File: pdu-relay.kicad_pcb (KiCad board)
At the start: 2 copper layers, 55 x 40 mm, 15 parts, among them J1 L_IN, J2 N, J3 L_OUT, J4 EXT_ON, K2 G2RL-1A-E DC5, Q1 BSS84PW

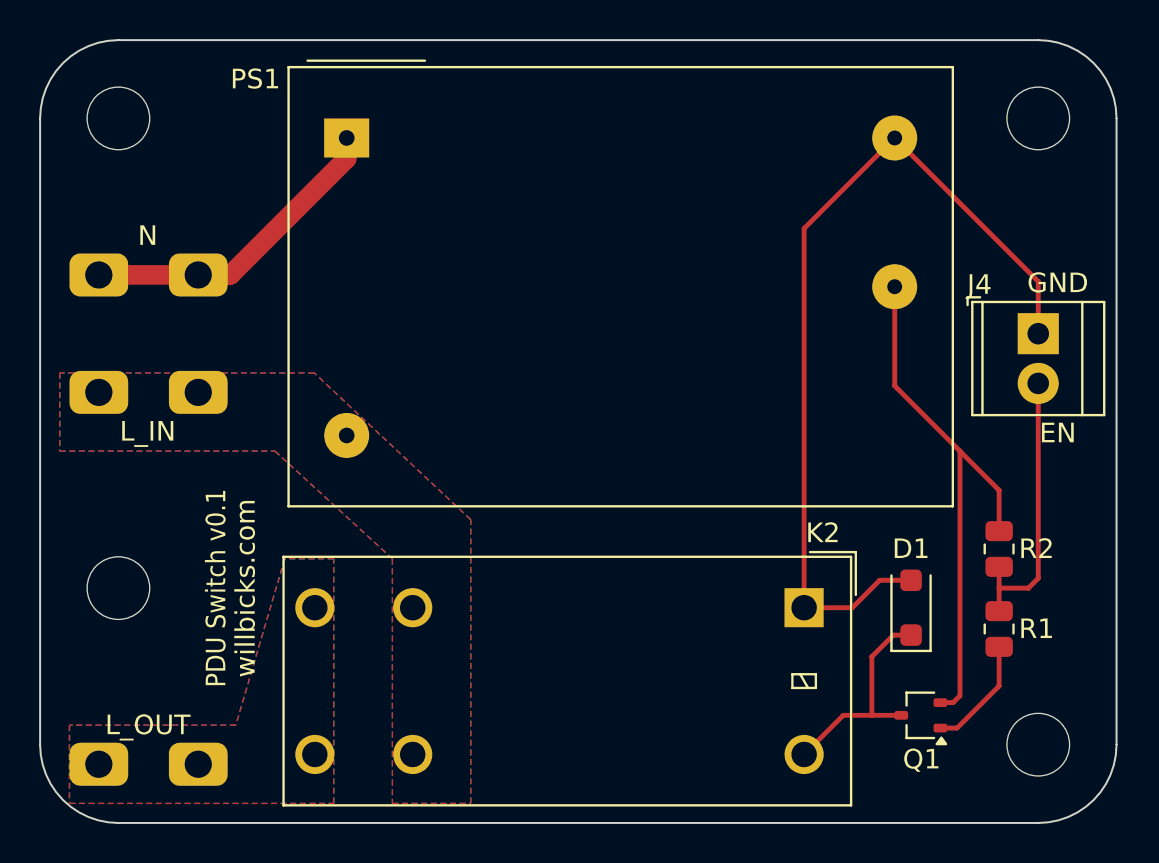
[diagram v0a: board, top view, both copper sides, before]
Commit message: Rearrange L_OUT for rectangular hole pattern and add 3D models.
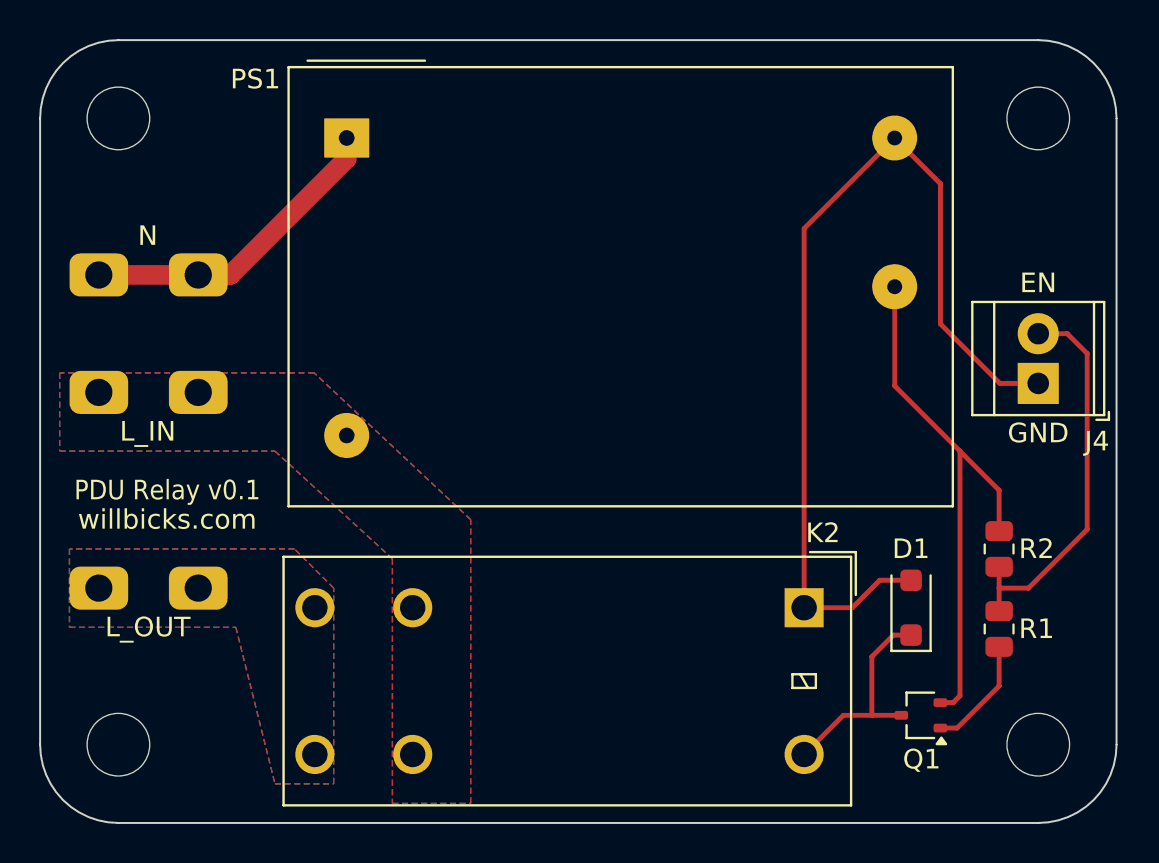
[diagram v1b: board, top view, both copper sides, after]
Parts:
- moved J3 9.00 mm to (92.5, 83.0)
- moved H3 8.00 mm to (91.0, 91.0)
- moved J4 2.54 mm to (138.0, 72.5), turned to 90 degrees
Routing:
- net Net-(J4-Pin_2): track 14.4 -> 19.9 mm
- net GND: track 45.0 -> 48.7 mm
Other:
- board text added: "PDU Relay v0.1"
- board text removed: "PDU Switch v0.1"

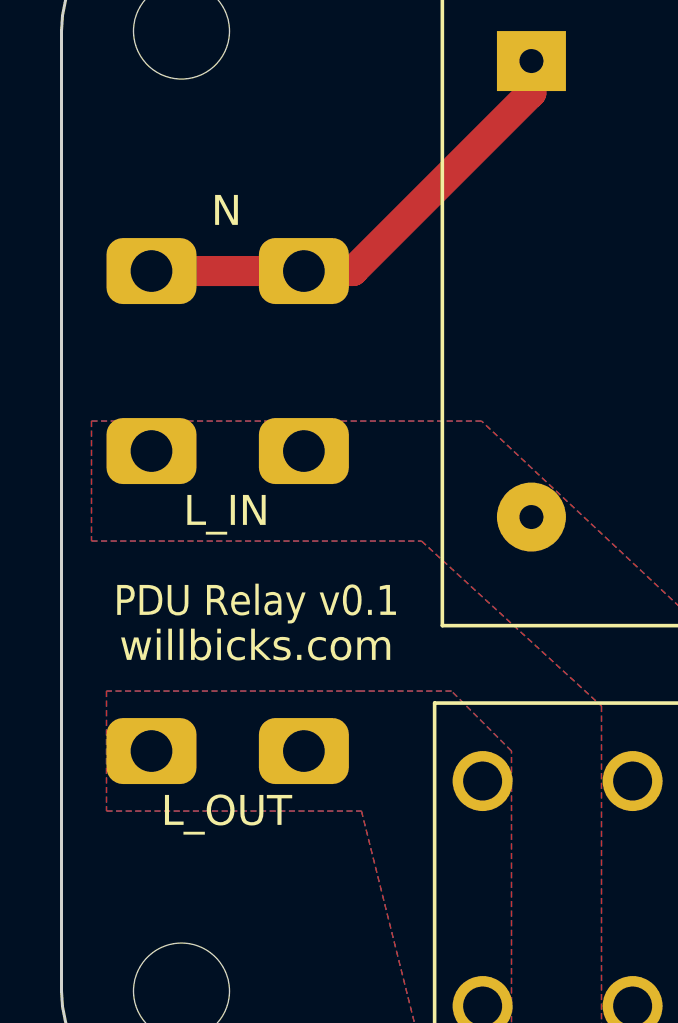
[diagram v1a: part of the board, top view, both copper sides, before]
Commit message: Add 3D model for spade terminals
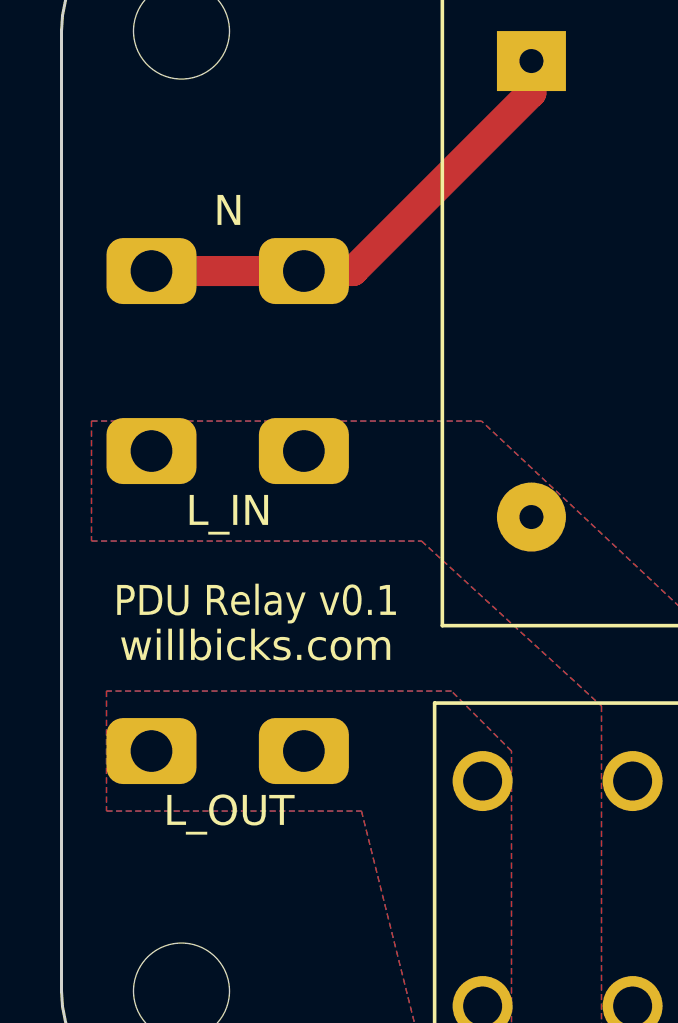
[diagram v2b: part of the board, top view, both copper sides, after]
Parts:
- turned J1 to 180 degrees
- turned J2 to 180 degrees
- turned J3 to 180 degrees
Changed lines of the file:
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@@
 			(drillshape 0)
 			(scaleselection 1)
-			(outputdirectory "")
+			(outputdirectory "out/PDU_Relay_v0-1_Gerbers/")
 		)
 	)
@@
 		(property ki_fp_filters "MountingHole*")
 		(sheetname "Root")
-		(sheetfile "pdu-switch.kicad_sch")
+		(sheetfile "pdu-relay.kicad_sch")
 		(attr exclude_from_pos_files)
 		(fp_circle
@@
 		(property ki_fp_filters "MountingHole*")
 		(sheetname "Root")
-		(sheetfile "pdu-switch.kicad_sch")
+		(sheetfile "pdu-relay.kicad_sch")
 		(attr exclude_from_pos_files)
 		(fp_circle
@@
 		(tags "THT Terminal Block TE 282834-2 pitch 2.54mm size 5.54x6.5mm^2 drill 1.1mm pad 2.1mm")
 		(property "Reference" "J4"
-			(at -2.96 3 360)
+			(at -2.96 3 0)
 			(layer "F.SilkS")
 			(effects
@@
 		)
 		(property "Value" "EXT_ON"
-			(at 1.27 4.37 270)
+			(at 1.27 4.37 -90)
 			(layer "F.Fab")
 			(effects
@@
 		(property ki_fp_filters "TerminalBlock*:*")
 		(sheetname "Root")
-		(sheetfile "pdu-switch.kicad_sch")
+		(sheetfile "pdu-relay.kicad_sch")
 		(attr through_hole)
 		(fp_line
@@
 		)
 		(fp_text user "${REFERENCE}"
-			(at 1.27 2 270)
+			(at 1.27 2 -90)
 			(layer "F.Fab")
 			(effects
@@
 		(property ki_fp_filters "R_*")
 		(sheetname "Root")
-		(sheetfile "pdu-switch.kicad_sch")
+		(sheetfile "pdu-relay.kicad_sch")
 		(attr smd)
 		(fp_line
@@
 		(property ki_fp_filters "Relay?SPST*")
 		(sheetname "Root")
-		(sheetfile "pdu-switch.kicad_sch")
+		(sheetfile "pdu-relay.kicad_sch")
 		(attr through_hole)
 		(fp_line
@@
 		(property ki_fp_filters "MountingHole*")
 		(sheetname "Root")
-		(sheetfile "pdu-switch.kicad_sch")
+		(sheetfile "pdu-relay.kicad_sch")
 		(attr exclude_from_pos_files)
 		(fp_circle
@@
 		(property ki_fp_filters "MountingHole*")
 		(sheetname "Root")
-		(sheetfile "pdu-switch.kicad_sch")
+		(sheetfile "pdu-relay.kicad_sch")
 		(attr exclude_from_pos_files)
 		(fp_circle
@@
 		)
 		(sheetname "Root")
-		(sheetfile "pdu-switch.kicad_sch")
+		(sheetfile "pdu-relay.kicad_sch")
 		(attr smd)
 		(fp_line
@@
 		(property ki_fp_filters "TO-???* *_Diode_* *SingleDiode* D_*")
 		(sheetname "Root")
-		(sheetfile "pdu-switch.kicad_sch")
+		(sheetfile "pdu-relay.kicad_sch")
 		(attr smd)
 		(fp_line
@@
 	(footprint "Connector_Spade:Keystone_4966"
 		(layer "F.Cu")
-		(at 92.54 73)
+		(at 92.54 73 180)
 		(property "Reference" "J1"
-			(at 0 -2 0)
+			(at 0 -2 180)
 			(unlocked yes)
 			(layer "F.SilkS")
@@
 		)
 		(property "Value" "L_IN"
-			(at -0.04 2 0)
+			(at -0.04 -2 0)
 			(unlocked yes)
 			(layer "F.SilkS")
@@
 		)
 		(property "Footprint" "Connector_Spade:Keystone_4966"
-			(at 0 0 0)
+			(at 0 0 180)
 			(unlocked yes)
 			(layer "F.Fab")
@@
 		)
 		(property "Datasheet" "https://www.mouser.com/datasheet/2/215/4966-743260.pdf"
-			(at 0 0 0)
+			(at 0 0 180)
 			(unlocked yes)
 			(layer "F.Fab")
@@
 		)
 		(property "Description" ""
-			(at 0 0 0)
-			(unlocked yes)
-			(layer "F.Fab")
-			(hide yes)
-			(effects
-				(font
-					(size 1 1)
-					(thickness 0.15)
-				)
-			)
-		)
-		(property ki_fp_filters "Connector*:*_1x??_*")
-		(sheetname "Root")
-		(sheetfile "pdu-switch.kicad_sch")
+			(at 0 0 180)
+			(unlocked yes)
+			(layer "F.Fab")
+			(hide yes)
+			(effects
+				(font
+					(size 1 1)
+					(thickness 0.15)
+				)
+			)
+		)
 		(attr through_hole)
 		(fp_rect
@@
 		)
 		(fp_text user "${REFERENCE}"
-			(at 0 3.5 0)
+			(at 0 3.5 180)
 			(unlocked yes)
 			(layer "F.Fab")
@@
 		)
 		(pad "1" thru_hole roundrect
-			(at -2.54 0)
+			(at -2.54 0 180)
 			(size 3 2.2)
 			(drill 1.39)
@@
 		)
 		(pad "1" thru_hole roundrect
-			(at 2.54 0)
+			(at 2.54 0 180)
 			(size 3 2.2)
 			(drill 1.39)
@@
 			(pintype "passive")
 		)
+		(model "${KIPRJMOD}/Connector_Spade.pretty/Keystone_4966.wrl"
+			(offset
+				(xyz 0 0 0)
+			)
+			(scale
+				(xyz 1 1 1)
+			)
+			(rotate
+				(xyz 0 0 0)
+			)
+		)
 	)
 	(footprint "Converter_ACDC:Converter_ACDC_MeanWell_IRM-02-xx_THT"
@@
 		(property ki_fp_filters "Converter*ACDC*MeanWell*IRM*02*THT*")
 		(sheetname "Root")
-		(sheetfile "pdu-switch.kicad_sch")
+		(sheetfile "pdu-relay.kicad_sch")
 		(attr through_hole)
 		(fp_line
@@
 	(footprint "Connector_Spade:Keystone_4966"
 		(layer "F.Cu")
-		(at 92.54 67)
+		(at 92.54 67 180)
 		(property "Reference" "J2"
-			(at 0 -2 0)
+			(at 0 -2 180)
 			(unlocked yes)
 			(layer "F.SilkS")
@@
 		)
 		(property "Value" "N"
-			(at -0.04 -2 0)
+			(at -0.039999 2.000001 0)
 			(unlocked yes)
 			(layer "F.SilkS")
@@
 		)
 		(property "Footprint" "Connector_Spade:Keystone_4966"
-			(at 0 0 0)
+			(at 0 0 180)
 			(unlocked yes)
 			(layer "F.Fab")
@@
 		)
 		(property "Datasheet" "https://www.mouser.com/datasheet/2/215/4966-743260.pdf"
-			(at 0 0 0)
+			(at 0 0 180)
 			(unlocked yes)
 			(layer "F.Fab")
@@
 		)
 		(property "Description" ""
-			(at 0 0 0)
-			(unlocked yes)
-			(layer "F.Fab")
-			(hide yes)
-			(effects
-				(font
-					(size 1 1)
-					(thickness 0.15)
-				)
-			)
-		)
-		(property ki_fp_filters "Connector*:*_1x??_*")
-		(sheetname "Root")
-		(sheetfile "pdu-switch.kicad_sch")
+			(at 0 0 180)
+			(unlocked yes)
+			(layer "F.Fab")
+			(hide yes)
+			(effects
+				(font
+					(size 1 1)
+					(thickness 0.15)
+				)
+			)
+		)
 		(attr through_hole)
 		(fp_rect
@@
 		)
 		(fp_text user "${REFERENCE}"
-			(at 0 3.5 0)
+			(at 0 3.5 180)
 			(unlocked yes)
 			(layer "F.Fab")
@@
 		)
 		(pad "1" thru_hole roundrect
-			(at -2.54 0)
+			(at -2.54 0 180)
 			(size 3 2.2)
 			(drill 1.39)
@@
 		)
 		(pad "1" thru_hole roundrect
-			(at 2.54 0)
+			(at 2.54 0 180)
 			(size 3 2.2)
 			(drill 1.39)
@@
 			(pintype "passive")
 		)
+		(model "${KIPRJMOD}/Connector_Spade.pretty/Keystone_4966.wrl"
+			(offset
+				(xyz 0 0 0)
+			)
+			(scale
+				(xyz 1 1 1)
+			)
+			(rotate
+				(xyz 0 0 0)
+			)
+		)
 	)
 	(footprint "Connector_Spade:Keystone_4966"
 		(layer "F.Cu")
-		(at 92.54 83)
+		(at 92.54 83 180)
 		(property "Reference" "J3"
-			(at 0 -2 0)
+			(at 0 -2 180)
 			(unlocked yes)
 			(layer "F.SilkS")
@@
 		)
 		(property "Value" "L_OUT"
-			(at -0.04 2 0)
+			(at -0.04 -2 0)
 			(unlocked yes)
 			(layer "F.SilkS")
@@
 		)
 		(property "Footprint" "Connector_Spade:Keystone_4966"
-			(at 0 0 0)
+			(at 0 0 180)
 			(unlocked yes)
 			(layer "F.Fab")
@@
 		)
 		(property "Datasheet" "https://www.mouser.com/datasheet/2/215/4966-743260.pdf"
-			(at 0 0 0)
+			(at 0 0 180)
 			(unlocked yes)
 			(layer "F.Fab")
@@
 		)
 		(property "Description" ""
-			(at 0 0 0)
-			(unlocked yes)
-			(layer "F.Fab")
-			(hide yes)
-			(effects
-				(font
-					(size 1 1)
-					(thickness 0.15)
-				)
-			)
-		)
-		(property ki_fp_filters "Connector*:*_1x??_*")
-		(sheetname "Root")
-		(sheetfile "pdu-switch.kicad_sch")
+			(at 0 0 180)
+			(unlocked yes)
+			(layer "F.Fab")
+			(hide yes)
+			(effects
+				(font
+					(size 1 1)
+					(thickness 0.15)
+				)
+			)
+		)
 		(attr through_hole)
 		(fp_rect
@@
 		)
 		(fp_text user "${REFERENCE}"
-			(at 0 3.5 0)
+			(at 0 3.5 180)
 			(unlocked yes)
 			(layer "F.Fab")
@@
 		)
 		(pad "1" thru_hole roundrect
-			(at -2.54 0)
+			(at -2.54 0 180)
 			(size 3 2.2)
 			(drill 1.39)
@@
 		)
 		(pad "1" thru_hole roundrect
-			(at 2.54 0)
+			(at 2.54 0 180)
 			(size 3 2.2)
 			(drill 1.39)
@@
 			(pintype "passive")
 		)
+		(model "${KIPRJMOD}/Connector_Spade.pretty/Keystone_4966.wrl"
+			(offset
+				(xyz 0 0 0)
+			)
+			(scale
+				(xyz 1 1 1)
+			)
+			(rotate
+				(xyz 0 0 0)
+			)
+		)
 	)
 	(footprint "Resistor_SMD:R_0805_2012Metric"
@@
 		(property ki_fp_filters "R_*")
 		(sheetname "Root")
-		(sheetfile "pdu-switch.kicad_sch")
+		(sheetfile "pdu-relay.kicad_sch")
 		(attr smd)
 		(fp_line
